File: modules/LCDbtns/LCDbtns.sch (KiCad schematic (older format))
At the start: 12 parts, among them J1 Conn_01x03_Male, J2 Conn_01x03_Male

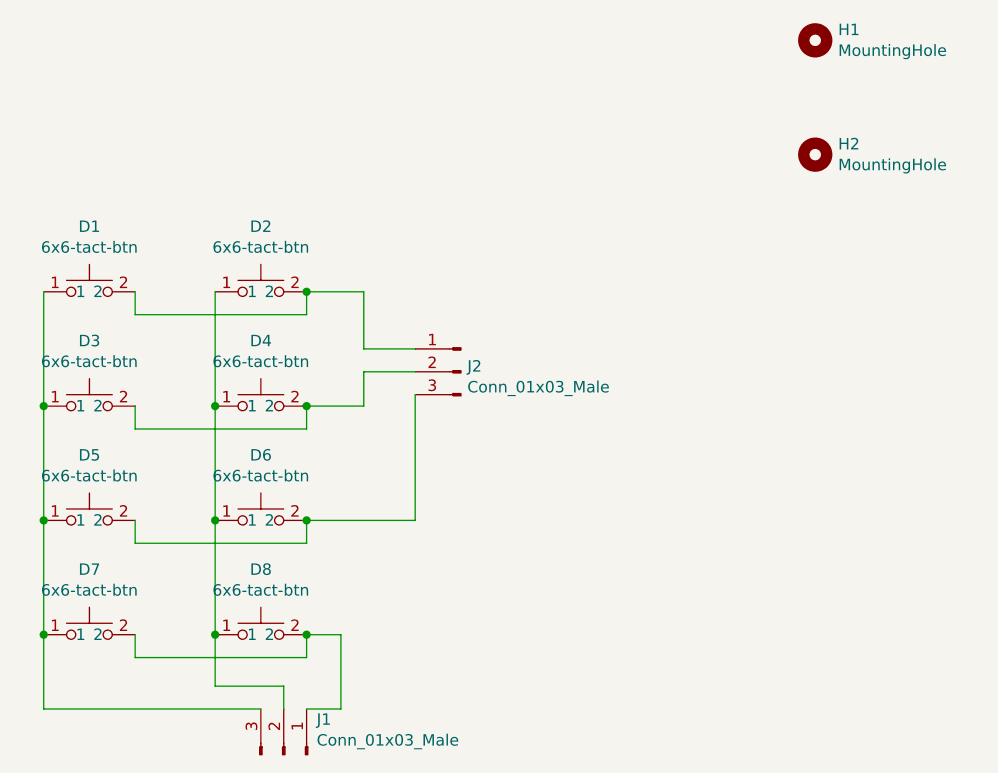
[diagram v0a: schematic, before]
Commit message: Add diodes to LCD btns PCB. Add gerber.
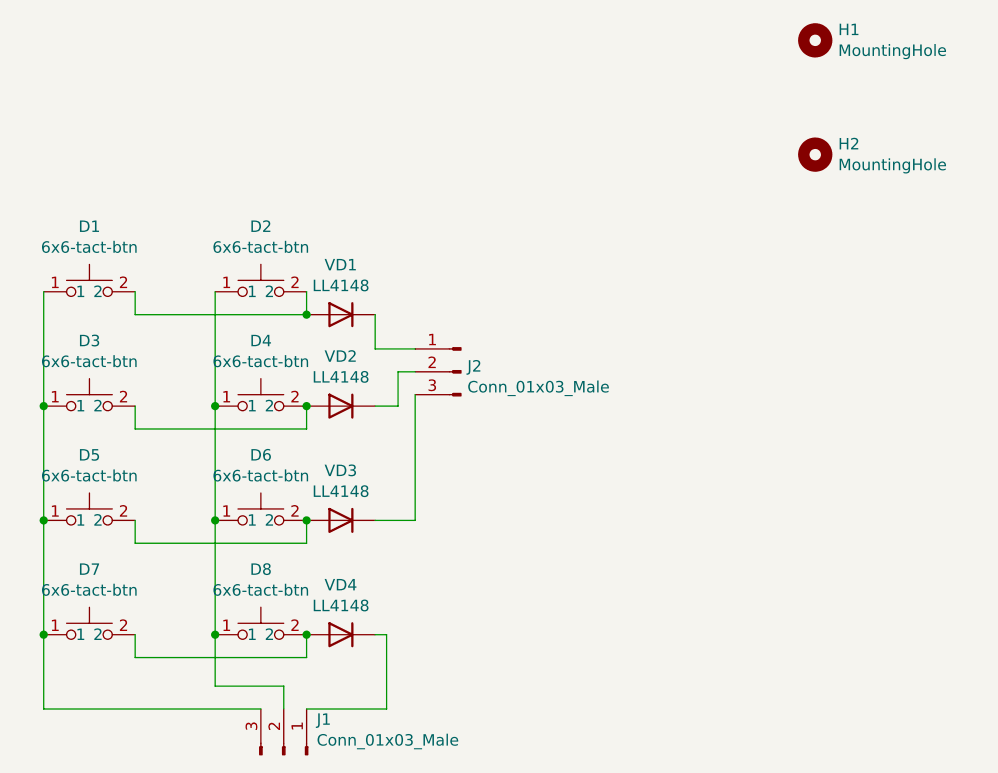
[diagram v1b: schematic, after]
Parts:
- added VD1, VD2, VD3, VD4: LL4148, Diode_SMD:D_MiniMELF, symbol Diode:LL4148
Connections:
- net at D5.2, D6.2: now also VD3.2 (A); no longer J2.3 (Pin_3)
- net at D3.2, D4.2: now also VD2.2 (A); no longer J2.2 (Pin_2)
- net at D1.2, D2.2: now also VD1.2 (A); no longer J2.1 (Pin_1)
- net at D7.2, D8.2: now also VD4.2 (A); no longer J1.1 (Pin_1)
- new net: J1.1 (Pin_1), VD4.1 (K)
- new net: J2.1 (Pin_1), VD1.1 (K)
- new net: J2.2 (Pin_2), VD2.1 (K)
- new net: J2.3 (Pin_3), VD3.1 (K)
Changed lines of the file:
@@
 EESchema Schematic File Version 4
-LIBS:LCDbtns-cache
 EELAYER 30 0
 EELAYER END
@@
 Connection ~ 2500 4500
 Wire Wire Line
-	2900 4500 3050 4500
-Wire Wire Line
-	3050 4500 3050 4825
-Wire Wire Line
-	3050 4825 2900 4825
+	3375 4000 3375 3450
+$Comp
+L Diode:LL4148 VD3
+U 1 1 5FBD5410
+P 3050 4000
+F 0 "VD3" H 3050 4217 50  0000 C CNN
+F 1 "LL4148" H 3050 4126 50  0000 C CNN
+F 2 "Diode_SMD:D_MiniMELF" H 3050 3825 50  0001 C CNN
+F 3 "http://www.vishay.com/docs/85557/ll4148.pdf" H 3050 4000 50  0001 C CNN
+	1    3050 4000
+	-1   0    0    -1
+$EndComp
+$Comp
+L Diode:LL4148 VD2
+U 1 1 5FBD68D6
+P 3050 3500
+F 0 "VD2" H 3050 3717 50  0000 C CNN
+F 1 "LL4148" H 3050 3626 50  0000 C CNN
+F 2 "Diode_SMD:D_MiniMELF" H 3050 3325 50  0001 C CNN
+F 3 "http://www.vishay.com/docs/85557/ll4148.pdf" H 3050 3500 50  0001 C CNN
+	1    3050 3500
+	-1   0    0    -1
+$EndComp
+Connection ~ 2900 3500
+Wire Wire Line
+	3200 3500 3300 3500
+Wire Wire Line
+	3300 3500 3300 3350
+Wire Wire Line
+	3300 3350 3375 3350
+$Comp
+L Diode:LL4148 VD1
+U 1 1 5FBD776B
+P 3050 3100
+F 0 "VD1" H 3050 3317 50  0000 C CNN
+F 1 "LL4148" H 3050 3226 50  0000 C CNN
+F 2 "Diode_SMD:D_MiniMELF" H 3050 2925 50  0001 C CNN
+F 3 "http://www.vishay.com/docs/85557/ll4148.pdf" H 3050 3100 50  0001 C CNN
+	1    3050 3100
+	-1   0    0    -1
+$EndComp
+Wire Wire Line
+	3200 3100 3200 3250
+Wire Wire Line
+	3200 3250 3375 3250
+$Comp
+L Diode:LL4148 VD4
+U 1 1 5FBD8089
+P 3050 4500
+F 0 "VD4" H 3050 4717 50  0000 C CNN
+F 1 "LL4148" H 3050 4626 50  0000 C CNN
+F 2 "Diode_SMD:D_MiniMELF" H 3050 4325 50  0001 C CNN
+F 3 "http://www.vishay.com/docs/85557/ll4148.pdf" H 3050 4500 50  0001 C CNN
+	1    3050 4500
+	-1   0    0    -1
+$EndComp
 Connection ~ 2900 4500
 Wire Wire Line
-	2900 4000 3375 4000
-Wire Wire Line
-	3375 4000 3375 3450
+	3200 4500 3250 4500
+Wire Wire Line
+	3250 4500 3250 4825
+Wire Wire Line
+	2900 4825 3250 4825
 Connection ~ 2900 4000
 Wire Wire Line
-	2900 3500 3150 3500
-Wire Wire Line
-	3150 3500 3150 3350
-Wire Wire Line
-	3150 3350 3375 3350
-Connection ~ 2900 3500
-Wire Wire Line
-	2900 3000 3150 3000
-Wire Wire Line
-	3150 3000 3150 3250
-Wire Wire Line
-	3150 3250 3375 3250
-Connection ~ 2900 3000
+	3200 4000 3375 4000
+Connection ~ 2900 3100
 $EndSCHEMATC

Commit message: LCD btns. Add pin names.
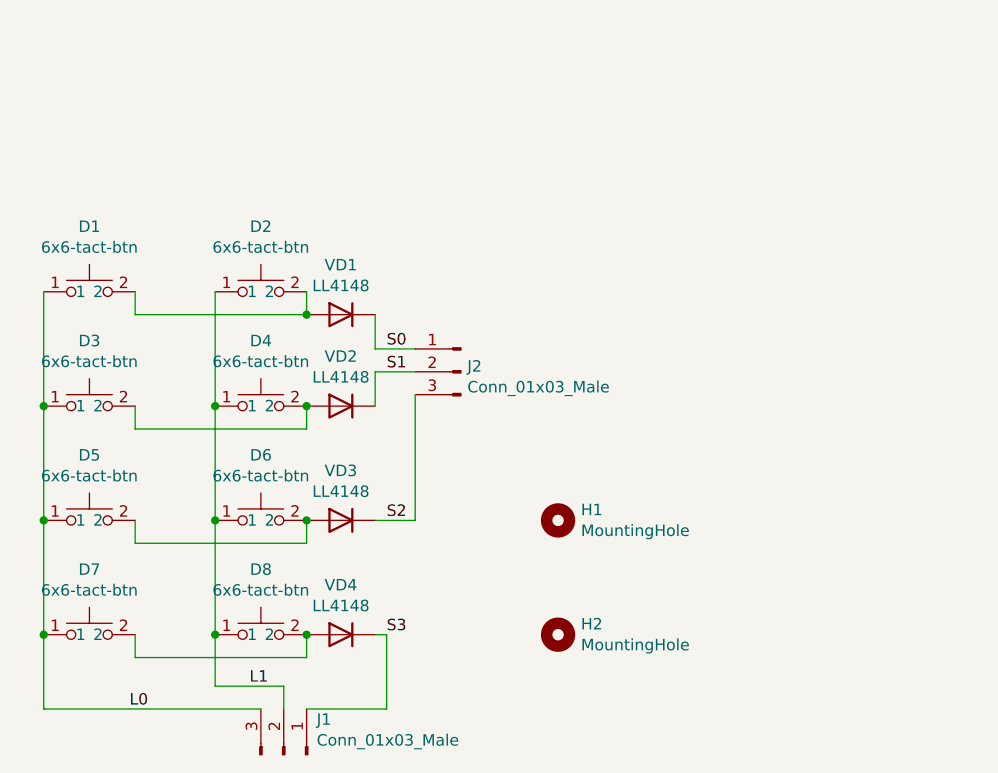
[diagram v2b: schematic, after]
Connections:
- net L0: now reaches D1.1, D3.1, D5.1, D7.1, J1.3 (Pin_3)
- net L1: now reaches D2.1, D4.1, D6.1, D8.1, J1.2 (Pin_2)
- net S3: now reaches J1.1 (Pin_1), VD4.1 (K)
- net S0: now reaches J2.1 (Pin_1), VD1.1 (K)
- net S1: now reaches J2.2 (Pin_2), VD2.1 (K)
- net S2: now reaches J2.3 (Pin_3), VD3.1 (K)
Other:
- moved on the sheet: H1, H2
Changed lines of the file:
@@
 L Mechanical:MountingHole H1
 U 1 1 5E9F03FE
-P 5125 1900
-F 0 "H1" H 5225 1946 50  0000 L CNN
-F 1 "MountingHole" H 5225 1855 50  0000 L CNN
-F 2 "MountingHole:MountingHole_3.2mm_M3" H 5125 1900 50  0001 C CNN
-F 3 "~" H 5125 1900 50  0001 C CNN
-	1    5125 1900
+P 4000 4000
+F 0 "H1" H 4100 4046 50  0000 L CNN
+F 1 "MountingHole" H 4100 3955 50  0000 L CNN
+F 2 "MountingHole:MountingHole_3.2mm_M3" H 4000 4000 50  0001 C CNN
+F 3 "~" H 4000 4000 50  0001 C CNN
+	1    4000 4000
 	1    0    0    -1
 $EndComp
@@
 L Mechanical:MountingHole H2
 U 1 1 5E9F0888
-P 5125 2400
-F 0 "H2" H 5225 2446 50  0000 L CNN
-F 1 "MountingHole" H 5225 2355 50  0000 L CNN
-F 2 "MountingHole:MountingHole_3.2mm_M3" H 5125 2400 50  0001 C CNN
-F 3 "~" H 5125 2400 50  0001 C CNN
-	1    5125 2400
+P 4000 4500
+F 0 "H2" H 4100 4546 50  0000 L CNN
+F 1 "MountingHole" H 4100 4455 50  0000 L CNN
+F 2 "MountingHole:MountingHole_3.2mm_M3" H 4000 4500 50  0001 C CNN
+F 3 "~" H 4000 4500 50  0001 C CNN
+	1    4000 4500
 	1    0    0    -1
 $EndComp
@@
 $EndComp
 Connection ~ 2900 3500
-Wire Wire Line
-	3200 3500 3300 3500
-Wire Wire Line
-	3300 3500 3300 3350
-Wire Wire Line
-	3300 3350 3375 3350
 $Comp
 L Diode:LL4148 VD1
@@
 	3200 4000 3375 4000
 Connection ~ 2900 3100
+Text Label 3250 3250 0    50   ~ 0
+S0
+Text Label 3250 3350 0    50   ~ 0
+S1
+Text Label 3250 4000 0    50   ~ 0
+S2
+Text Label 3250 4500 0    50   ~ 0
+S3
+Text Label 2125 4825 0    50   ~ 0
+L0
+Text Label 2650 4725 0    50   ~ 0
+L1
+Wire Wire Line
+	3200 3350 3200 3500
+Wire Wire Line
+	3200 3350 3375 3350
 $EndSCHEMATC
